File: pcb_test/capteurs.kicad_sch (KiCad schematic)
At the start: 14 parts, among them U10 BMP581, U8 BMM350, U9 BMI323

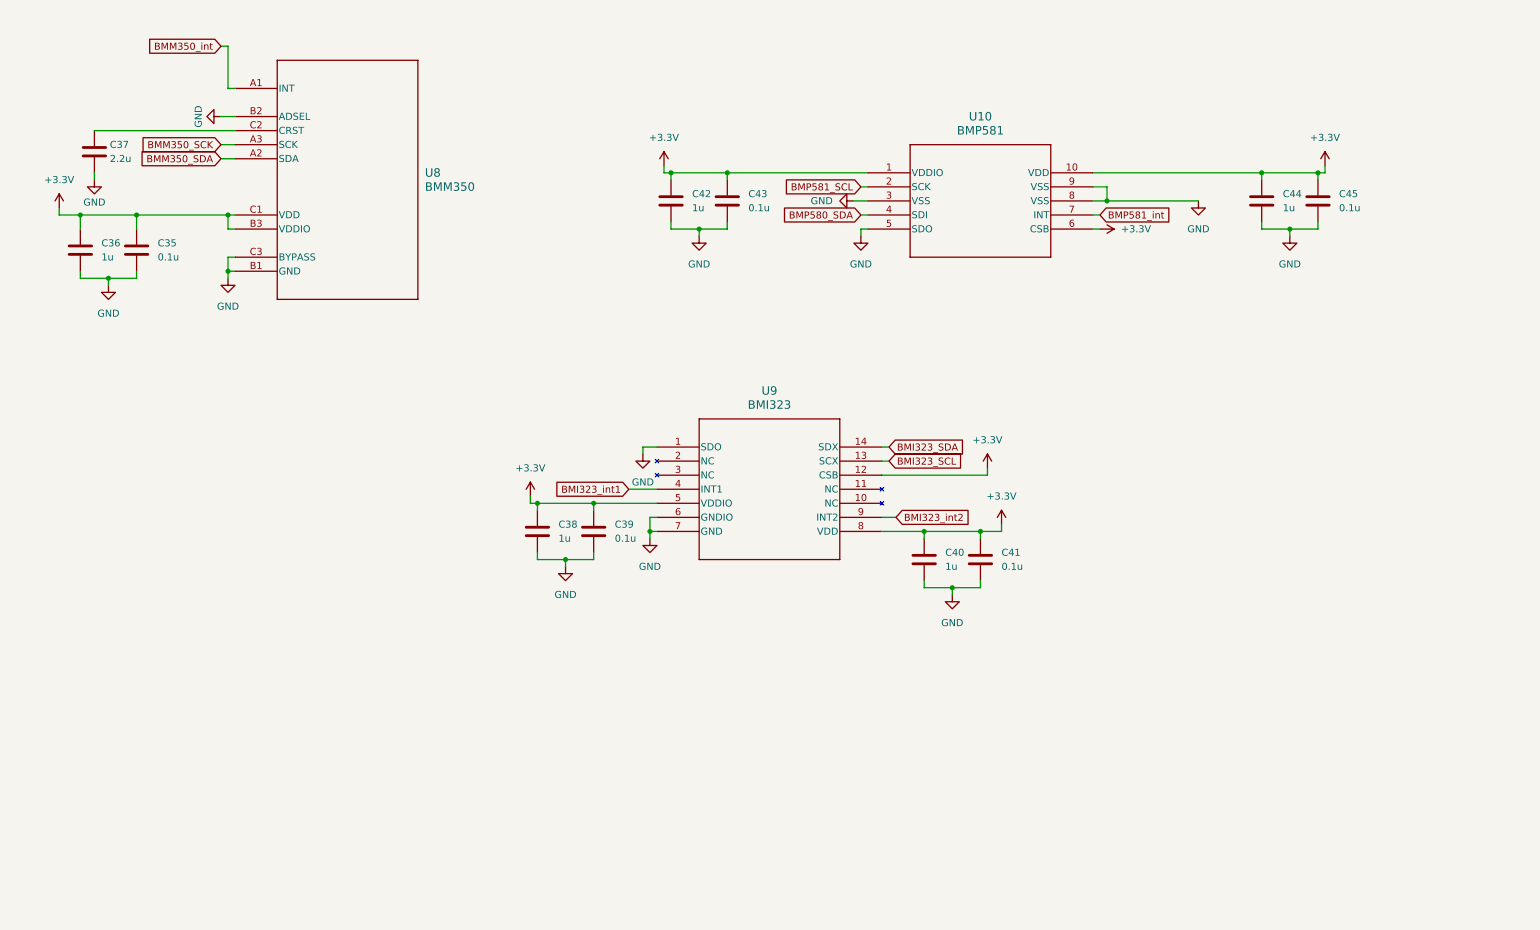
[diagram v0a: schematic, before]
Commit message: Ajout GPS, retrait radio, clean up schemas
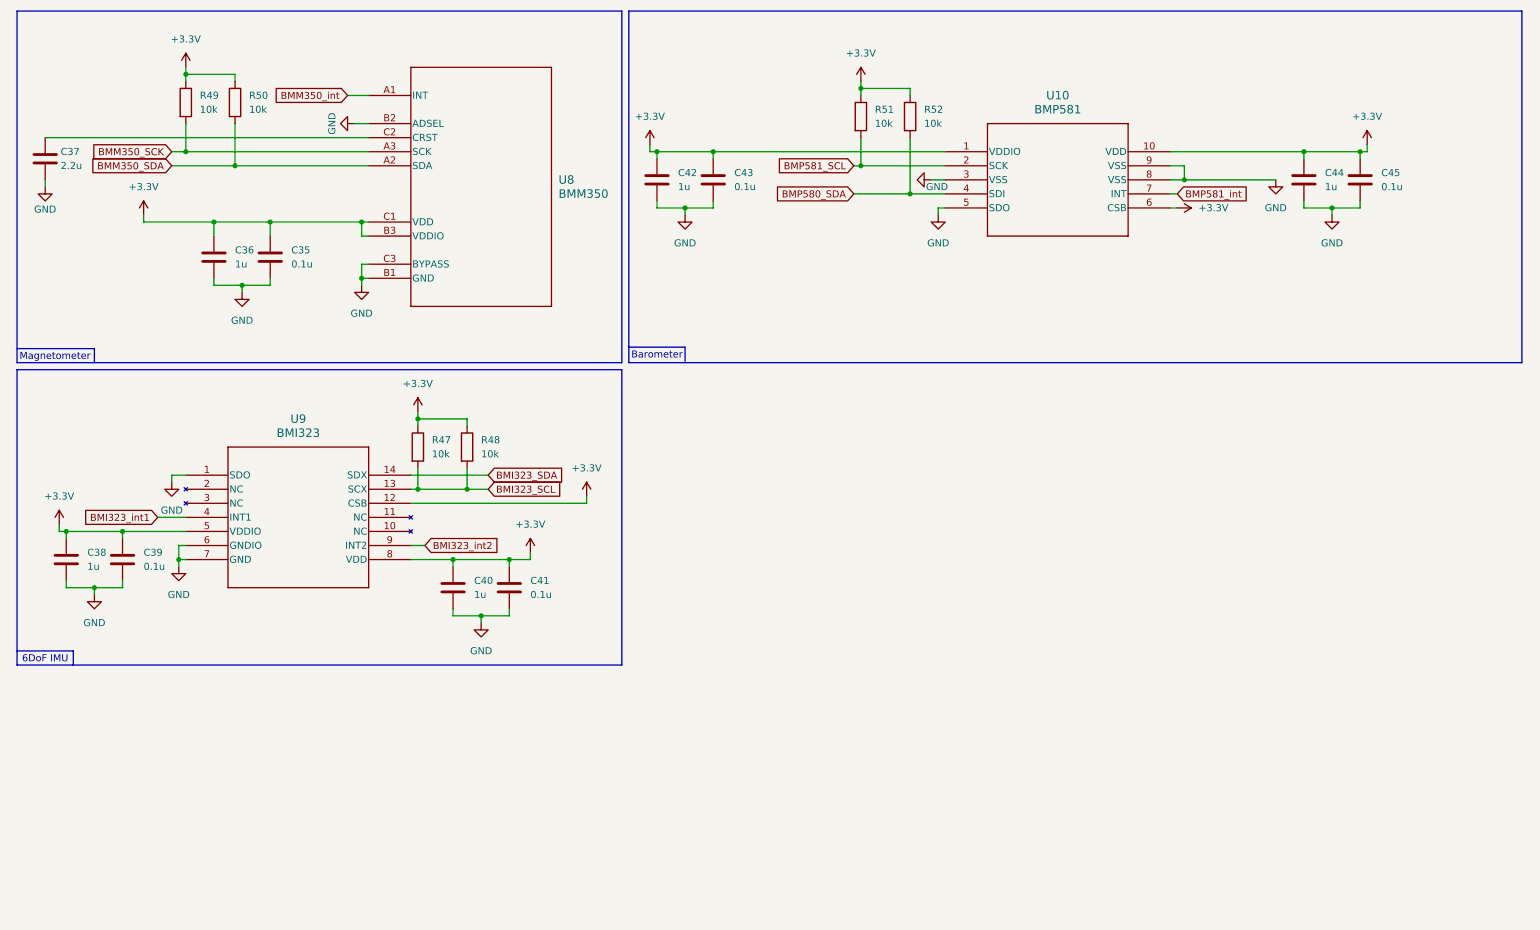
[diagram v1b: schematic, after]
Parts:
- added R47, R48, R49, R50, R51, R52: 10k, symbol Device:R
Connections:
- net +3.3V: now also R47.1, R48.1, R49.1, R50.1, R51.1, R52.1
- net BMI323_SCL: now also R47.2, R48.2
- net BMM350_SCK: now also R49.2
- net BMM350_SDA: now also R50.2
- net BMP580_SDA: now also R52.2
- net BMP581_SCL: now also R51.2
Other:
- note added: "6DoF IMU"
- note added: "Barometer"
- note added: "Magnetometer"
- moved on the sheet: C35, C36, C37, C38, C39, C40, C41, C42, C43, C44, C45, U10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

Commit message: Ajout testpoints
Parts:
- added TP44, TP45, TP46, TP47, TP48, TP49, TP50, TP51, TP52, TP53, TP54, TP55, TP56: TestPoint, symbol Connector:TestPoint
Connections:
- net BMI323_SCL: now also TP48.1
- net BMI323_SDA: now also TP49.1
- net BMI323_int1: now also TP50.1
- net BMI323_int2: now also TP52.1
- net BMM350_SCK: now also TP44.1
- net BMM350_SDA: now also TP45.1
- net BMM350_int: now also TP46.1
- net BMP580_SDA: now also TP54.1
- net BMP581_SCL: now also TP53.1
- net BMP581_int: now also TP55.1
- net GND: now also TP47.1, TP51.1, TP56.1

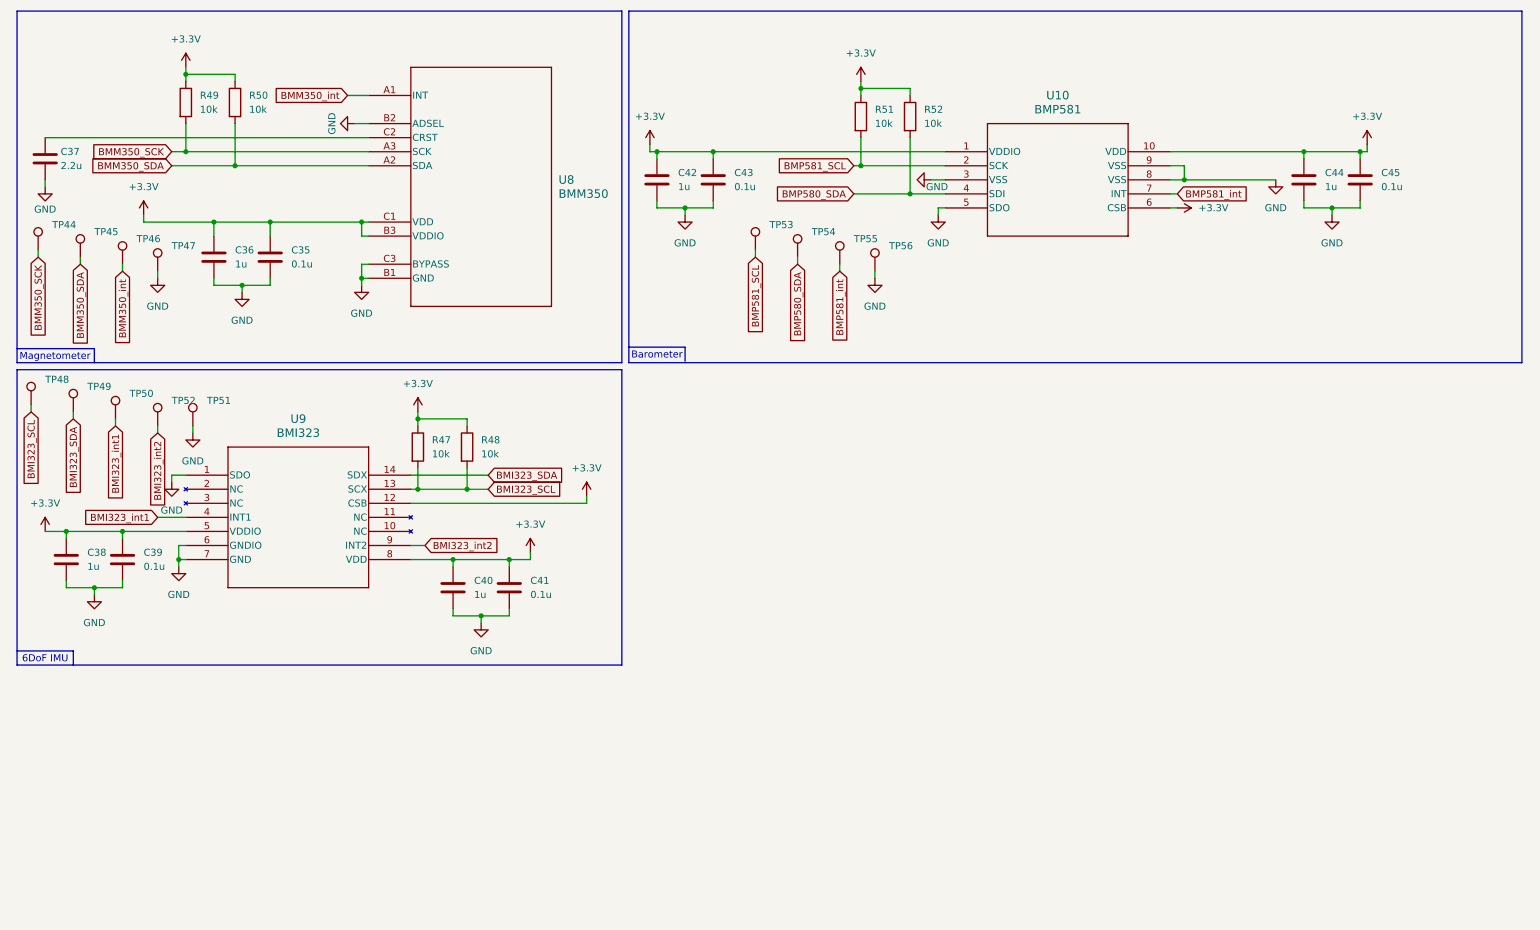
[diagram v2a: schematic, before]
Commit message: refait alimentation, changement MCU, separation schema eMMC/octospi, reajout RF
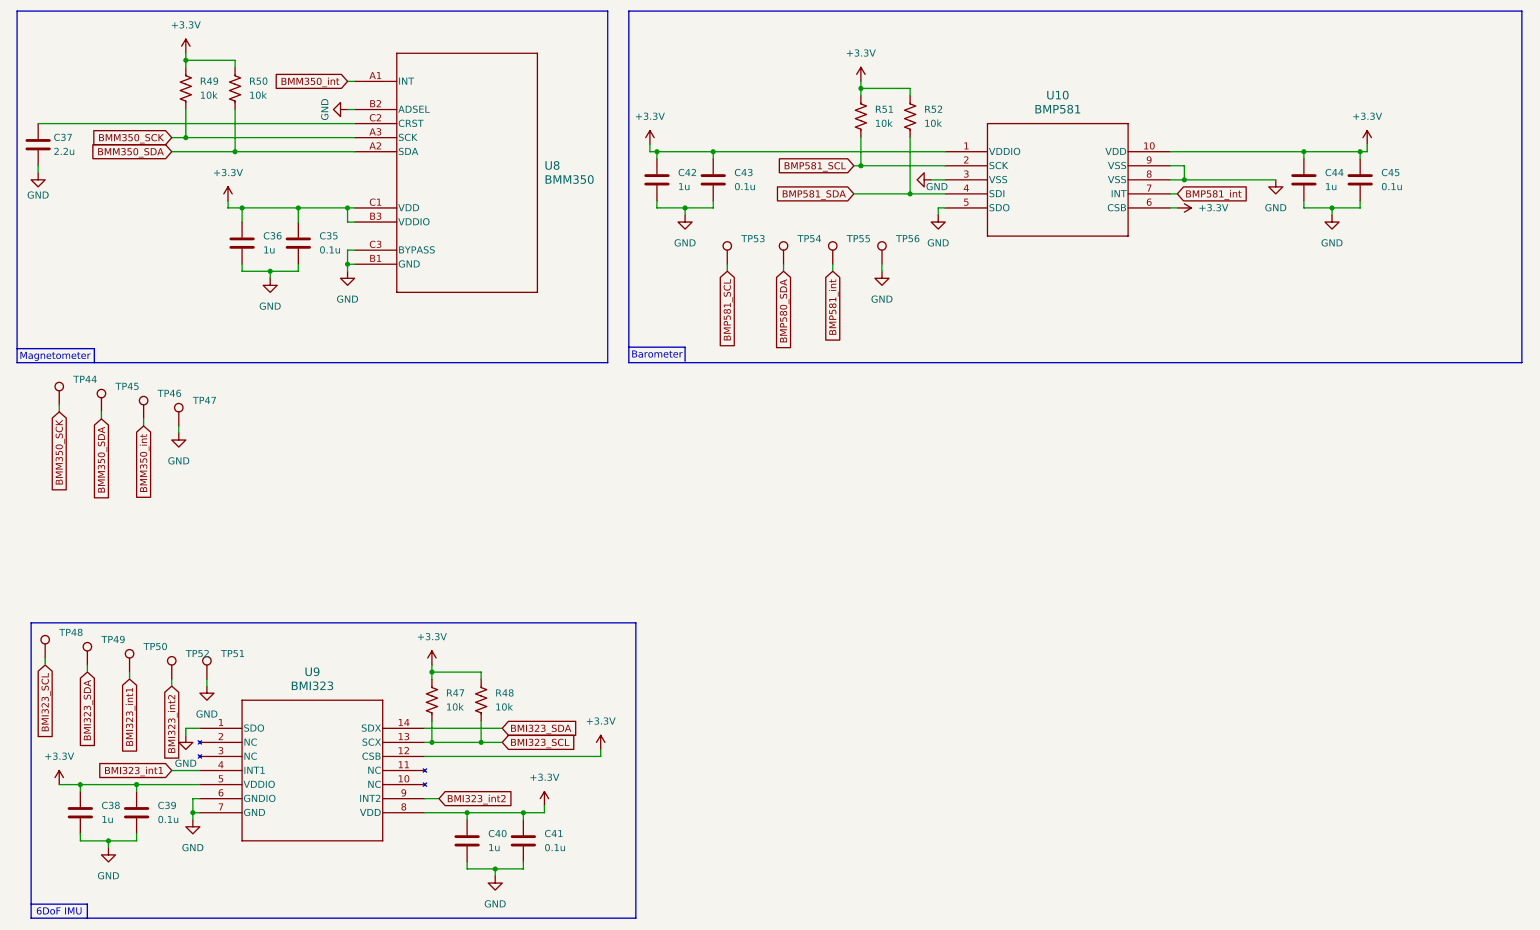
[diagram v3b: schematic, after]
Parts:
- R47, R48, R49, R50, R51, R52: symbol Device:R -> Device:R_US
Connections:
- net BMP580_SDA: no longer R52.2, U10.4 (SDI)
- new net BMP581_SDA: R52.2, U10.4 (SDI)
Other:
- moved on the sheet: C35, C36, C37, C38, C39, C40, C41, TP44, TP45, TP46, TP47, TP48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

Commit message: alimentation finale. Retouches testpoints et condo decouplage, finalisation requis, ajout sheet finale.
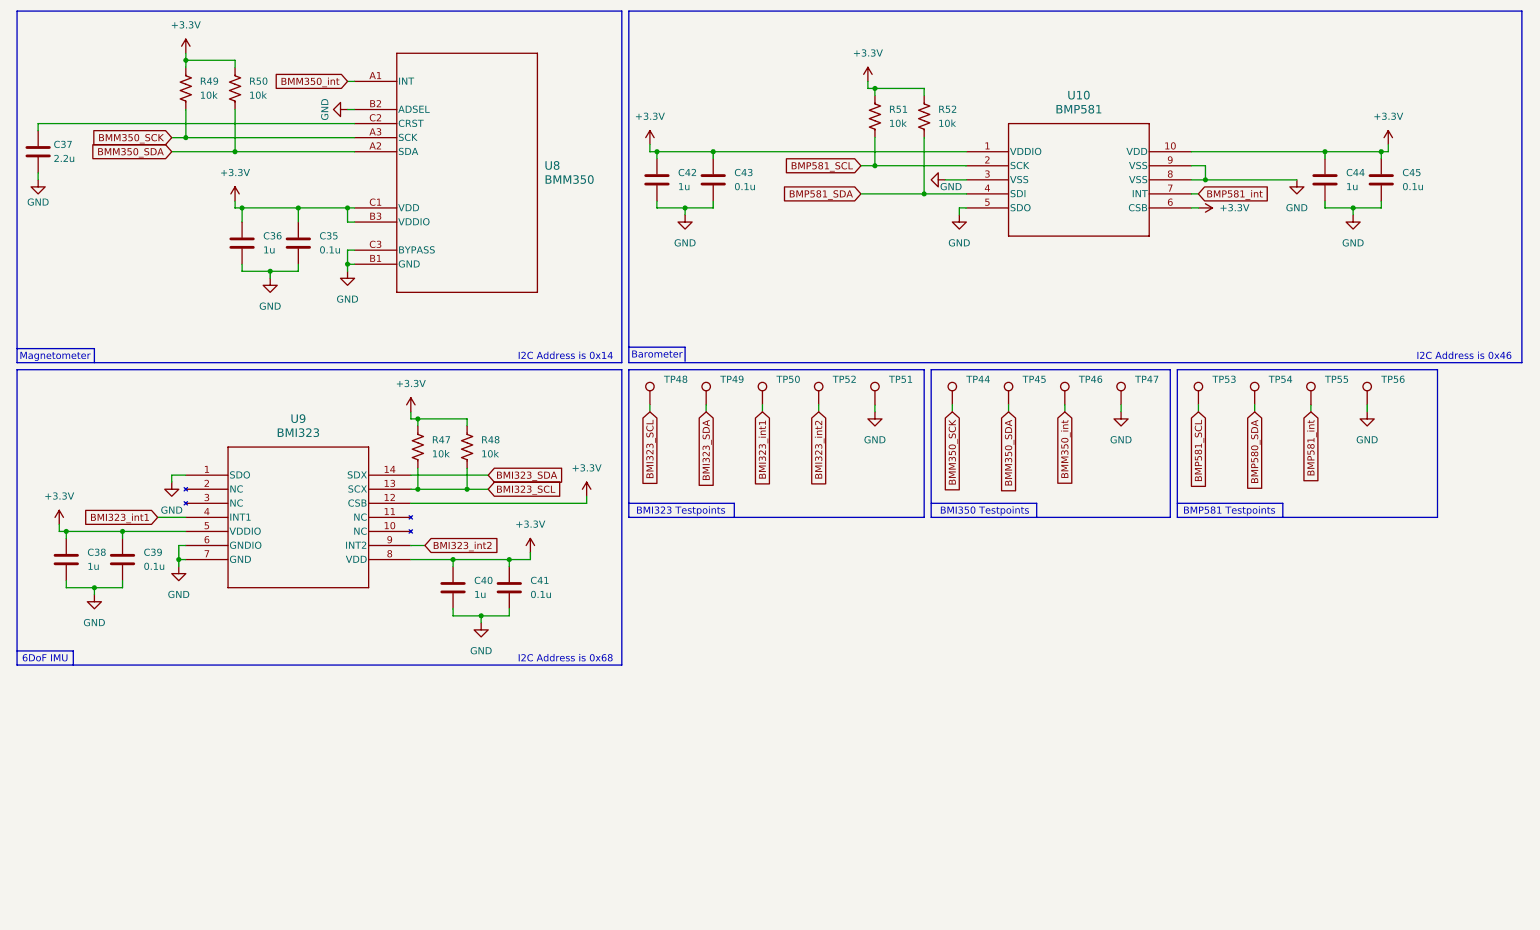
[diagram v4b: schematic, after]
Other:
- note added: "BMI323 Testpoints"
- note added: "BMI350 Testpoints"
- note added: "BMP581 Testpoints"
- note added: "I2C Address is 0x14"
- note added: "I2C Address is 0x46"
- note added: "I2C Address is 0x68"
- moved on the sheet: C37, C38, C39, C40, C41, C44, C45, R47, R48, R51, R52, TP44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
